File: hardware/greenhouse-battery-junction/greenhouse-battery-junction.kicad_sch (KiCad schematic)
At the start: 7 parts, among them J1 Conn_01x10_Female, J10 Conn_01x03_Female, J11 Screw_Terminal_01x02, J12 Conn_01x04_Male, J13 Screw_Terminal_01x02, J2 Conn_01x03_Female

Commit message: Add TODO to battery junction
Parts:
- added J?: Screw_Terminal_01x02, TerminalBlock_Phoenix:TerminalBlock_Phoenix_MKDS-1,5-2-5.08_1x02_P5.08mm_Horizontal, symbol Connector:Screw_Terminal_01x02
- added R? (x2): R_US, symbol Device:R_US
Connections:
- net ADC_A0: now also R?.1, R?.2
- net Current_Out: now also J?.2 (Pin_2)
- net GND: now also J?.1 (Pin_1), R?.2
- net Current_In renamed +12V
- net +12V: now also R?.1
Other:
- note added: "TODO: Turn voltage divider off when not measuring voltage."
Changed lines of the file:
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@@
 (kicad_sch (version 20211123) (generator eeschema)
   (paper "A4")
+  (junction (at 91.44 45.72) (diameter 0) (color 0 0 0 0)
+  )
   (junction (at 82.55 93.98) (diameter 0) (color 0 0 0 0)
   )
+  (junction (at 115.57 62.23) (diameter 0) (color 0 0 0 0)
+  )
   (junction (at 82.55 104.14) (diameter 0) (color 0 0 0 0)
   )
+  (junction (at 91.44 35.56) (diameter 0) (color 0 0 0 0)
+  )
   (junction (at 82.55 134.62) (diameter 0) (color 0 0 0 0)
   )
@@
     (stroke (width 0) (type default) (color 0 0 0 0))
   )
+  (wire (pts (xy 106.68 62.23) (xy 115.57 62.23))
+    (stroke (width 0) (type default) (color 0 0 0 0))
+  )
+  (wire (pts (xy 60.96 43.18) (xy 74.93 43.18))
+    (stroke (width 0) (type default) (color 0 0 0 0))
+  )
   (wire (pts (xy 82.55 93.98) (xy 82.55 104.14))
     (stroke (width 0) (type default) (color 0 0 0 0))
@@
     (stroke (width 0) (type default) (color 0 0 0 0))
   )
-  (wire (pts (xy 78.74 38.1) (xy 78.74 39.37))
+  (wire (pts (xy 91.44 38.1) (xy 91.44 45.72))
     (stroke (width 0) (type default) (color 0 0 0 0))
   )
@@
     (stroke (width 0) (type default) (color 0 0 0 0))
   )
+  (wire (pts (xy 91.44 45.72) (xy 91.44 49.53))
+    (stroke (width 0) (type default) (color 0 0 0 0))
+  )
   (wire (pts (xy 55.88 116.84) (xy 85.09 116.84))
     (stroke (width 0) (type default) (color 0 0 0 0))
@@
     (stroke (width 0) (type default) (color 0 0 0 0))
   )
-  (wire (pts (xy 60.96 38.1) (xy 78.74 38.1))
+  (wire (pts (xy 115.57 60.96) (xy 115.57 62.23))
+    (stroke (width 0) (type default) (color 0 0 0 0))
+  )
+  (wire (pts (xy 60.96 38.1) (xy 91.44 38.1))
     (stroke (width 0) (type default) (color 0 0 0 0))
   )
@@
     (stroke (width 0) (type default) (color 0 0 0 0))
   )
+  (wire (pts (xy 91.44 29.21) (xy 91.44 35.56))
+    (stroke (width 0) (type default) (color 0 0 0 0))
+  )
+  (wire (pts (xy 60.96 45.72) (xy 91.44 45.72))
+    (stroke (width 0) (type default) (color 0 0 0 0))
+  )
   (wire (pts (xy 55.88 129.54) (xy 80.01 129.54))
     (stroke (width 0) (type default) (color 0 0 0 0))
@@
     (stroke (width 0) (type default) (color 0 0 0 0))
   )
+  (wire (pts (xy 88.9 35.56) (xy 91.44 35.56))
+    (stroke (width 0) (type default) (color 0 0 0 0))
+  )
   (wire (pts (xy 55.88 93.98) (xy 82.55 93.98))
     (stroke (width 0) (type default) (color 0 0 0 0))
@@
     (stroke (width 0) (type default) (color 0 0 0 0))
   )
+  (wire (pts (xy 91.44 35.56) (xy 123.19 35.56))
+    (stroke (width 0) (type default) (color 0 0 0 0))
+  )
   (wire (pts (xy 55.88 134.62) (xy 82.55 134.62))
     (stroke (width 0) (type default) (color 0 0 0 0))
   )
+  (wire (pts (xy 115.57 62.23) (xy 115.57 63.5))
+    (stroke (width 0) (type default) (color 0 0 0 0))
+  )
   (wire (pts (xy 82.55 83.82) (xy 82.55 93.98))
     (stroke (width 0) (type default) (color 0 0 0 0))
   )
-  (wire (pts (xy 88.9 35.56) (xy 123.19 35.56))
-    (stroke (width 0) (type default) (color 0 0 0 0))
-  )
   (wire (pts (xy 123.19 33.02) (xy 110.49 33.02))
     (stroke (width 0) (type default) (color 0 0 0 0))
   )
+  (text "TODO: Turn voltage divider off\nwhen not measuring voltage."
+    (at 125.73 63.5 0)
+    (effects (font (size 1.27 1.27)) (justify left bottom))
+  )
   (label "ADC_SCL" (at 76.2 99.06 180)
     (effects (font (size 1.27 1.27)) (justify right bottom))
   )
-  (label "Input+12V" (at 102.87 35.56 180)
+  (label "Input+12V" (at 105.41 35.56 180)
     (effects (font (size 1.27 1.27)) (justify right bottom))
   )
@@
   )
   (label "ADC_VCC" (at 76.2 104.14 180)
+    (effects (font (size 1.27 1.27)) (justify right bottom))
+  )
+  (label "Current_Out" (at 74.93 43.18 180)
     (effects (font (size 1.27 1.27)) (justify right bottom))
   )
@@
   (label "ADC_GND" (at 76.2 101.6 180)
     (effects (font (size 1.27 1.27)) (justify right bottom))
+  )
+  (label "Volts_A" (at 106.68 62.23 0)
+    (effects (font (size 1.27 1.27)) (justify left bottom))
   )
   (label "Current_In" (at 110.49 35.56 0)
@@
     (pin "9")
   )
+  (symbol (lib_id "Device:R_US") (at 115.57 57.15 0) (unit 1)
+    (in_bom yes) (on_board yes) (fields_autoplaced)
+    (property "Reference" "R?" (id 0) (at 118.11 55.8799 0)
+      (effects (font (size 1.27 1.27)) (justify left))
+    )
+    (property "Value" "R_US" (id 1) (at 118.11 58.4199 0)
+      (effects (font (size 1.27 1.27)) (justify left))
+    )
+    (property "Footprint" "" (id 2) (at 116.586 57.404 90)
+      (effects (font (size 1.27 1.27)) hide)
+    )
+    (property "Datasheet" "~" (id 3) (at 115.57 57.15 0)
+      (effects (font (size 1.27 1.27)) hide)
+    )
+    (pin "1")
+    (pin "2")
+  )
+  (symbol (lib_id "power:+12V") (at 91.44 29.21 0) (unit 1)
+    (in_bom yes) (on_board yes) (fields_autoplaced)
+    (property "Reference" "#PWR?" (id 0) (at 91.44 33.02 0)
+      (effects (font (size 1.27 1.27)) hide)
+    )
+    (property "Value" "+12V" (id 1) (at 91.44 24.13 0))
+    (property "Footprint" "" (id 2) (at 91.44 29.21 0)
+      (effects (font (size 1.27 1.27)) hide)
+    )
+    (property "Datasheet" "" (id 3) (at 91.44 29.21 0)
+      (effects (font (size 1.27 1.27)) hide)
+    )
+    (pin "1")
+  )
+  (symbol (lib_id "Connector:Screw_Terminal_01x02") (at 55.88 45.72 180) (unit 1)
+    (in_bom yes) (on_board yes) (fields_autoplaced)
+    (property "Reference" "J?" (id 0) (at 53.34 43.1799 0)
+      (effects (font (size 1.27 1.27)) (justify left))
+    )
+    (property "Value" "Screw_Terminal_01x02" (id 1) (at 53.34 45.7199 0)
+      (effects (font (size 1.27 1.27)) (justify left))
+    )
+    (property "Footprint" "TerminalBlock_Phoenix:TerminalBlock_Phoenix_MKDS-1,5-2-5.08_1x02_P5.08mm_Horizontal" (id 2) (at 55.88 45.72 0)
+      (effects (font (size 1.27 1.27)) hide)
+    )
+    (property "Datasheet" "~" (id 3) (at 55.88 45.72 0)
+      (effects (font (size 1.27 1.27)) hide)
+    )
+    (pin "1")
+    (pin "2")
+  )
   (symbol (lib_id "Connector:Screw_Terminal_01x02") (at 55.88 38.1 180) (unit 1)
     (in_bom yes) (on_board yes) (fields_autoplaced)
@@
     (pin "1")
     (pin "2")
+  )
+  (symbol (lib_id "Device:R_US") (at 115.57 67.31 0) (unit 1)
+    (in_bom yes) (on_board yes) (fields_autoplaced)
+    (property "Reference" "R?" (id 0) (at 118.11 66.0399 0)
+      (effects (font (size 1.27 1.27)) (justify left))
+    )
+    (property "Value" "R_US" (id 1) (at 118.11 68.5799 0)
+      (effects (font (size 1.27 1.27)) (justify left))
+    )
+    (property "Footprint" "" (id 2) (at 116.586 67.564 90)
+      (effects (font (size 1.27 1.27)) hide)
+    )
+    (property "Datasheet" "~" (id 3) (at 115.57 67.31 0)
+      (effects (font (size 1.27 1.27)) hide)
+    )
+    (pin "1")
+    (pin "2")
+  )
+  (symbol (lib_id "power:GND") (at 115.57 71.12 0) (unit 1)
+    (in_bom yes) (on_board yes) (fields_autoplaced)
+    (property "Reference" "#PWR?" (id 0) (at 115.57 77.47 0)
+      (effects (font (size 1.27 1.27)) hide)
+    )
+    (property "Value" "GND" (id 1) (at 115.57 76.2 0))
+    (property "Footprint" "" (id 2) (at 115.57 71.12 0)
+      (effects (font (size 1.27 1.27)) hide)
+    )
+    (property "Datasheet" "" (id 3) (at 115.57 71.12 0)
+      (effects (font (size 1.27 1.27)) hide)
+    )
+    (pin "1")
+  )
+  (symbol (lib_id "power:+12V") (at 115.57 53.34 0) (unit 1)
+    (in_bom yes) (on_board yes) (fields_autoplaced)
+    (property "Reference" "#PWR?" (id 0) (at 115.57 57.15 0)
+      (effects (font (size 1.27 1.27)) hide)
+    )
+    (property "Value" "+12V" (id 1) (at 115.57 48.26 0))
+    (property "Footprint" "" (id 2) (at 115.57 53.34 0)
+      (effects (font (size 1.27 1.27)) hide)
+    )
+    (property "Datasheet" "" (id 3) (at 115.57 53.34 0)
+      (effects (font (size 1.27 1.27)) hide)
+    )
+    (pin "1")
   )
   (symbol (lib_id "power:+3.3V") (at 82.55 83.82 0) (unit 1)
@@
     (pin "2")
   )
-  (symbol (lib_id "power:GND") (at 78.74 39.37 0) (unit 1)
-    (in_bom yes) (on_board yes) (fields_autoplaced)
-    (property "Reference" "#PWR0129" (id 0) (at 78.74 45.72 0)
-      (effects (font (size 1.27 1.27)) hide)
-    )
-    (property "Value" "GND" (id 1) (at 78.74 44.45 0))
-    (property "Footprint" "" (id 2) (at 78.74 39.37 0)
-      (effects (font (size 1.27 1.27)) hide)
-    )
-    (property "Datasheet" "" (id 3) (at 78.74 39.37 0)
+  (symbol (lib_id "power:GND") (at 91.44 49.53 0) (unit 1)
+    (in_bom yes) (on_board yes) (fields_autoplaced)
+    (property "Reference" "#PWR0129" (id 0) (at 91.44 55.88 0)
+      (effects (font (size 1.27 1.27)) hide)
+    )
+    (property "Value" "GND" (id 1) (at 91.44 54.61 0))
+    (property "Footprint" "" (id 2) (at 91.44 49.53 0)
+      (effects (font (size 1.27 1.27)) hide)
+    )
+    (property "Datasheet" "" (id 3) (at 91.44 49.53 0)
       (effects (font (size 1.27 1.27)) hide)
     )
@@
       (reference "#PWR0132") (unit 1) (value "GND") (footprint "")
     )
+    (path "/29e1de3b-5bd3-4757-a0ec-3e4934fe5b16"
+      (reference "#PWR?") (unit 1) (value "+12V") (footprint "")
+    )
+    (path "/61acccc5-70cc-44d4-8908-c5dcdc7ba34f"
+      (reference "#PWR?") (unit 1) (value "GND") (footprint "")
+    )
+    (path "/626b0ced-0cbd-4abd-a932-165b811011c7"
+      (reference "#PWR?") (unit 1) (value "+12V") (footprint "")
+    )
     (path "/6ea06f35-328b-4023-b0c8-577506471241"
       (reference "#PWR?") (unit 1) (value "+3.3V") (footprint "")
@@
       (reference "J13") (unit 1) (value "Screw_Terminal_01x02") (footprint "TerminalBlock_Phoenix:TerminalBlock_Phoenix_MKDS-1,5-2-5.08_1x02_P5.08mm_Horizontal")
     )
-  )
+    (path "/48ff184a-cee2-4be5-9999-0ddbe9c67c45"
+      (reference "J?") (unit 1) (value "Screw_Terminal_01x02") (footprint "TerminalBlock_Phoenix:TerminalBlock_Phoenix_MKDS-1,5-2-5.08_1x02_P5.08mm_Horizontal")
+    )
+    (path "/28da386a-c4aa-4e3e-8b81-a8addeaadab5"
+      (reference "R?") (unit 1) (value "R_US") (footprint "")
+    )
+    (path "/60780b8d-67e5-45fb-920e-8c56b1dd11de"
+      (reference "R?") (unit 1) (value "R_US") (footprint "")
+    )
+  )

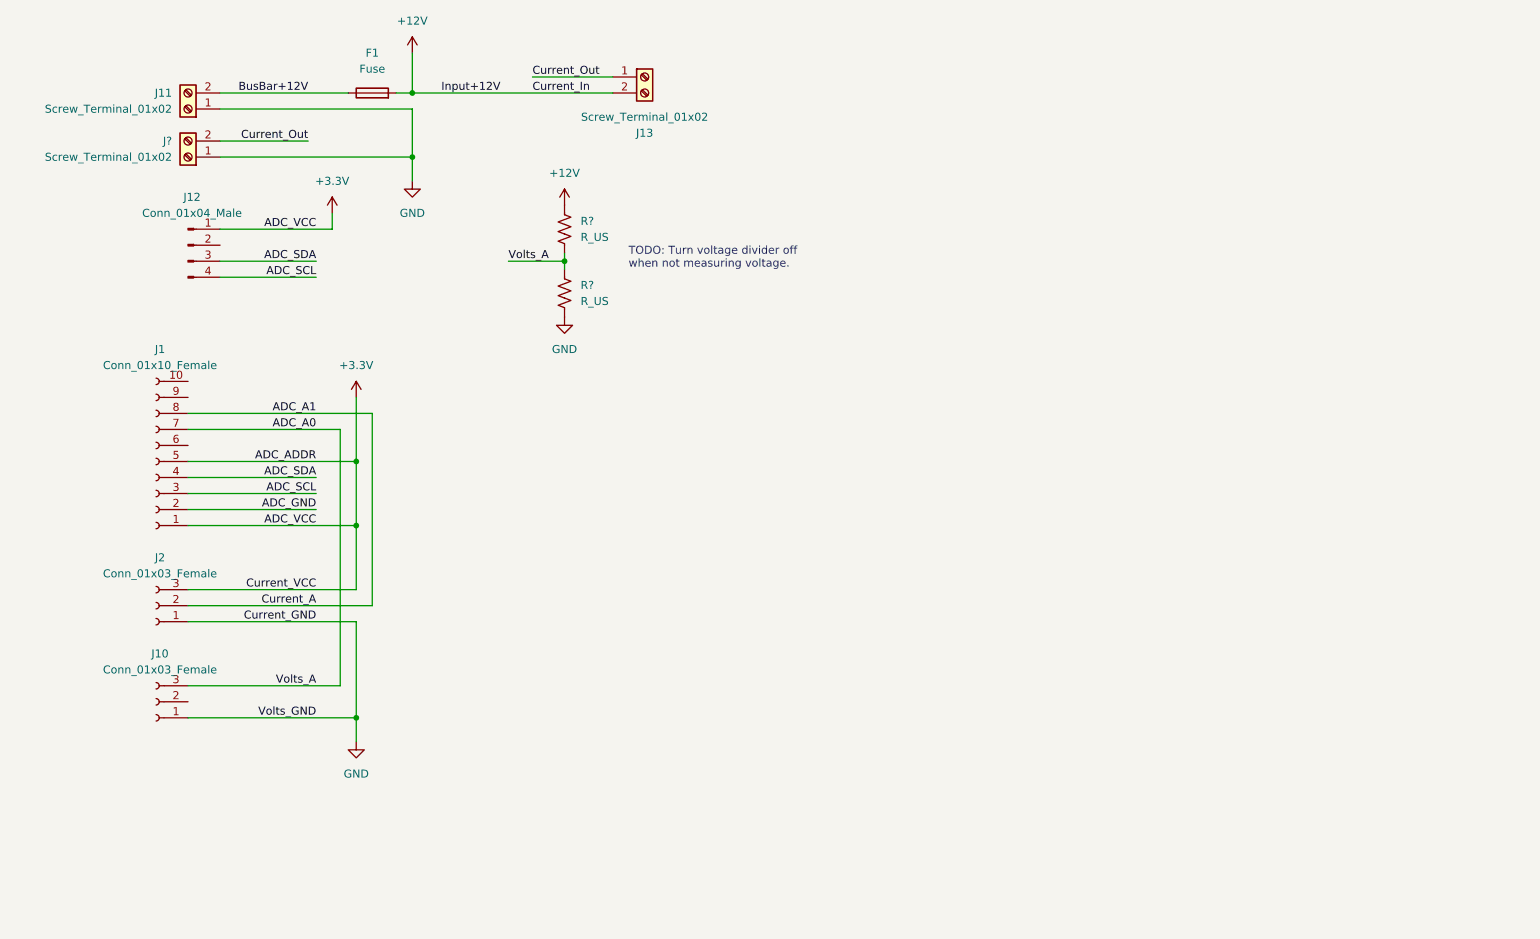
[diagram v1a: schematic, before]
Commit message: Voltage sensor and light switch
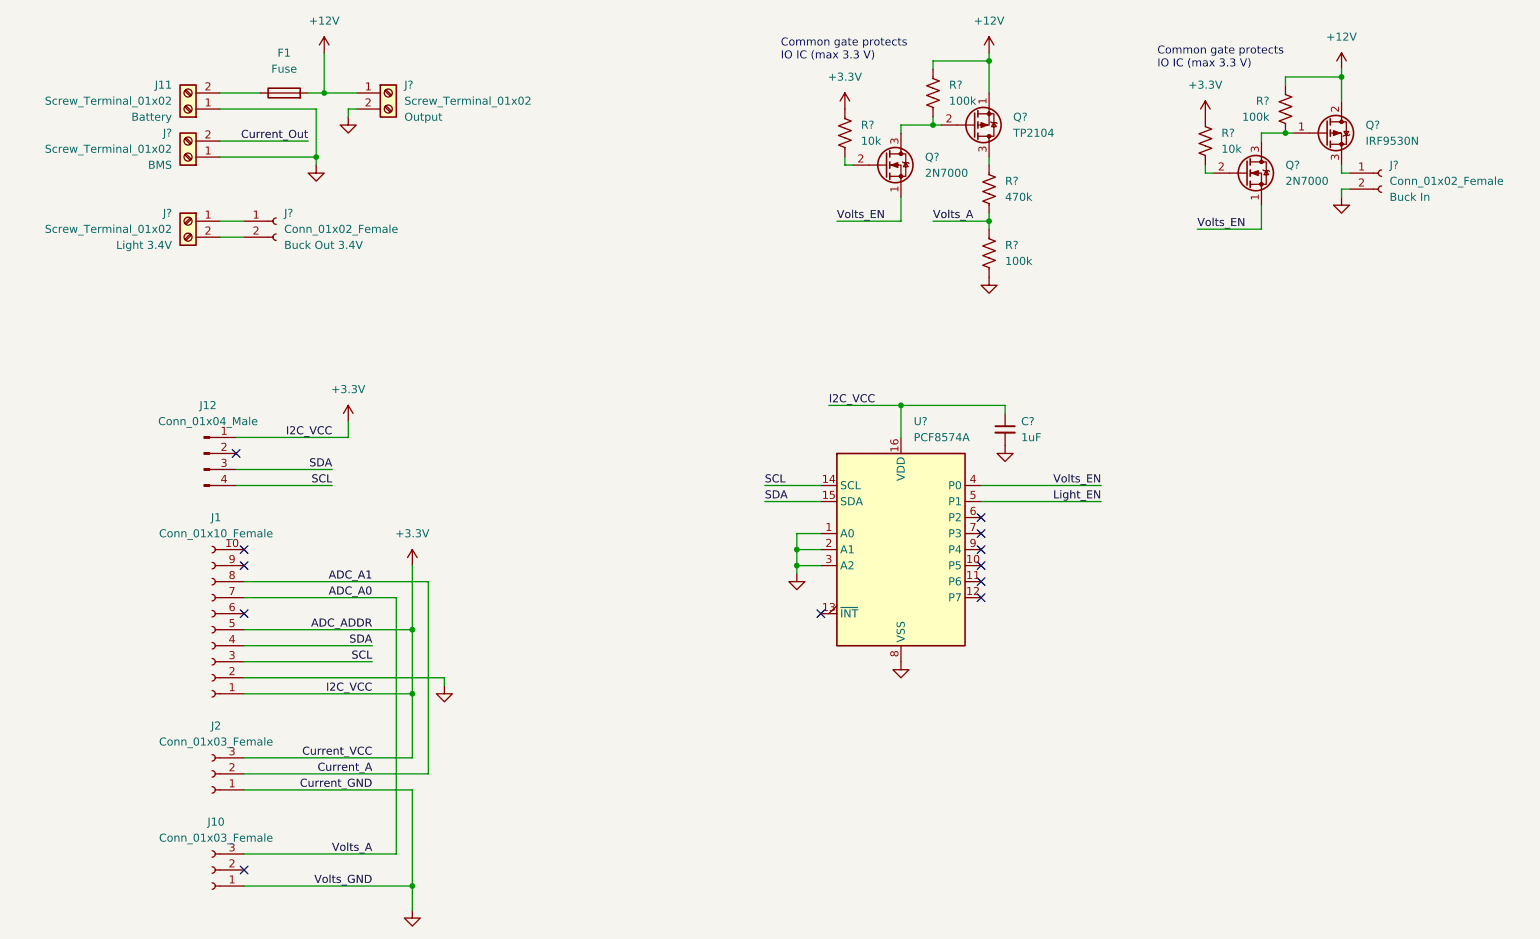
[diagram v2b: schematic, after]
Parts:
- removed J13: Screw_Terminal_01x02, TerminalBlock_Phoenix:TerminalBlock_Phoenix_MKDS-1,5-2-5.08_1x02_P5.08mm_Horizontal, symbol Connector:Screw_Terminal_01x02
- removed R? (x2): R_US, symbol Device:R_US
- added C?: 1uF, symbol Device:C_Small
- added J? (x2): Conn_01x02_Female, Connector_PinHeader_2.54mm:PinHeader_1x03_P2.54mm_Vertical, symbol Connector:Conn_01x02_Female
- added J? (x2): Screw_Terminal_01x02, TerminalBlock_Phoenix:TerminalBlock_Phoenix_MKDS-1,5-2-5.08_1x02_P5.08mm_Horizontal, symbol Connector:Screw_Terminal_01x02
- added Q?: TP2104, Package_TO_SOT_THT:TO-92_Inline, symbol Device:Q_PMOS_SGD
- added Q? (x2): 2N7000, Package_TO_SOT_THT:TO-92_Inline, symbol Transistor_FET:2N7000
- added Q?: IRF9530N, Package_TO_SOT_THT:TO-220-3_Vertical, symbol Transistor_FET:IRF9540N
- added R? (x2): 10k, symbol Device:R_US
- added R? (x3): 100k, symbol Device:R_US
- added R?: 470k, symbol Device:R_US
- added U?: PCF8574A, symbol Interface_Expansion:PCF8574A
- J11: Label (none) -> Battery
- J?: Label (none) -> BMS
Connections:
- net ADC_GND is gone; now on net GND: J1.2 (Pin_2)
- net +12V: now also J?.1 (Pin_1), Q?.1 (S), Q?.2 (D), R?.1, R?.1
- net +3V3: now also C?.1, R?.1, R?.1, U?.16 (VDD)
- net ADC_A0: now also R?.1, R?.2
- net GND: now also C?.2, J?.2 (Pin_2), J?.2 (Pin_2), R?.2, U?.1 (A0), U?.2 (A1), U?.3 (A2), U?.8 (VSS)
- net ADC_SCL renamed SCL
- net SCL: now also U?.14 (SCL)
- net ADC_SDA renamed SDA
- net SDA: now also U?.15 (SDA)
- net BusBar+12V: no longer names the net of F1.1, J11.2 (Pin_2)
- new net: Q?.2 (G), Q?.3 (D), R?.2
- new net: Q?.3 (D), R?.1
- new net: Q?.2 (G), R?.2 (x2)
- new net: J?.1 (Pin_1), J?.1 (Pin_1)
- new net: J?.2 (Pin_2), J?.2 (Pin_2)
- new net: J?.1 (Pin_1), Q?.3 (S)
- new net: Q?.1 (G), Q?.3 (D), R?.2
- new net Light_EN: U?.5 (P1)
- new net Volts_EN: Q?.1 (S), Q?.1 (S), U?.4 (P0)
- no-connect marks 0 -> 12
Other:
- note added: "Common gate protects IO IC (max 3.3 V)"
- note removed: "TODO: Turn voltage divider off when not measuring voltage."
- moved on the sheet: F1, J1, J10, J12, J2
